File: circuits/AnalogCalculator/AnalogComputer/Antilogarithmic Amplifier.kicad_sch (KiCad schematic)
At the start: 9 parts, among them U4 LM324

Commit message: update circuits
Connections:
- net +12V renamed VCC
- net -12V renamed VSS
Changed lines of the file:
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@@
-    )
-  )
-  (symbol (lib_id "power:+12V") (at 200.66 64.77 0) (unit 1)
-    (in_bom yes) (on_board yes) (dnp no) (fields_autoplaced)
-    (property "Reference" "#PWR04" (at 200.66 68.58 0)
-      (effects (font (size 1.27 1.27)) hide)
-    )
-    (property "Value" "+12V" (at 200.66 61.1942 0)
-      (effects (font (size 1.27 1.27)))
-    )
-    (property "Footprint" "" (at 200.66 64.77 0)
-      (effects (font (size 1.27 1.27)) hide)
-    )
-    (property "Datasheet" "" (at 200.66 64.77 0)
-      (effects (font (size 1.27 1.27)) hide)
-    )
-    (pin "1")
-    (instances
-      (project "AnalogComputer"
-        (path "/923be781-3164-4152-815e-8f20a1ba1c2e/bf1d90c3-cd96-4c8a-a7fb-5bc8190138ca"
-          (reference "#PWR04") (unit 1)
-        )
-        (path "/923be781-3164-4152-815e-8f20a1ba1c2e/3352ab9f-8e2e-464b-bae3-d09535b5c95b"
-          (reference "#PWR013") (unit 1)
-        )
-        (path "/923be781-3164-4152-815e-8f20a1ba1c2e/ca3b0da7-cf56-4357-ae82-a0a8c945f5f8"
-          (reference "#PWR016") (unit 1)
-        )
-      )
     )
   )
@@
     )
   )
+  (symbol (lib_id "power:VSS") (at 215.9 64.77 0) (unit 1)
+    (in_bom yes) (on_board yes) (dnp no) (fields_autoplaced)
+    (property "Reference" "#PWR014" (at 215.9 68.58 0)
+      (effects (font (size 1.27 1.27)) hide)
+    )
+    (property "Value" "VSS" (at 215.9 61.2681 0)
+      (effects (font (size 1.27 1.27)))
+    )
+    (property "Footprint" "" (at 215.9 64.77 0)
+      (effects (font (size 1.27 1.27)) hide)
+    )
+    (property "Datasheet" "" (at 215.9 64.77 0)
+      (effects (font (size 1.27 1.27)) hide)
+    )
+    (pin "1")
+    (instances
+      (project "AnalogComputer"
+        (path "/923be781-3164-4152-815e-8f20a1ba1c2e/bf1d90c3-cd96-4c8a-a7fb-5bc8190138ca"
+          (reference "#PWR014") (unit 1)
+        )
+        (path "/923be781-3164-4152-815e-8f20a1ba1c2e/3352ab9f-8e2e-464b-bae3-d09535b5c95b"
+          (reference "#PWR016") (unit 1)
+        )
+        (path "/923be781-3164-4152-815e-8f20a1ba1c2e/ca3b0da7-cf56-4357-ae82-a0a8c945f5f8"
+          (reference "#PWR017") (unit 1)
+        )
+      )
+    )
+  )
+  (symbol (lib_id "power:VCC") (at 200.66 64.77 0) (unit 1)
+    (in_bom yes) (on_board yes) (dnp no) (fields_autoplaced)
+    (property "Reference" "#PWR04" (at 200.66 68.58 0)
+      (effects (font (size 1.27 1.27)) hide)
+    )
+    (property "Value" "VCC" (at 200.66 61.2681 0)
+      (effects (font (size 1.27 1.27)))
+    )
+    (property "Footprint" "" (at 200.66 64.77 0)
+      (effects (font (size 1.27 1.27)) hide)
+    )
+    (property "Datasheet" "" (at 200.66 64.77 0)
+      (effects (font (size 1.27 1.27)) hide)
+    )
+    (pin "1")
+    (instances
+      (project "AnalogComputer"
+        (path "/923be781-3164-4152-815e-8f20a1ba1c2e/bf1d90c3-cd96-4c8a-a7fb-5bc8190138ca"
+          (reference "#PWR04") (unit 1)
+        )
+        (path "/923be781-3164-4152-815e-8f20a1ba1c2e/3352ab9f-8e2e-464b-bae3-d09535b5c95b"
+          (reference "#PWR05") (unit 1)
+        )
+        (path "/923be781-3164-4152-815e-8f20a1ba1c2e/ca3b0da7-cf56-4357-ae82-a0a8c945f5f8"
+          (reference "#PWR013") (unit 1)
+        )
+      )
+    )
+  )
   (symbol (lib_id "Device:R") (at 144.78 96.52 90) (unit 1)
     (in_bom yes) (on_board yes) (dnp no) (fields_autoplaced)
@@
         )
       )
-    )
-  )
-  (symbol (lib_id "power:-12V") (at 215.9 64.77 0) (unit 1)
-    (in_bom yes) (on_board yes) (dnp no) (fields_autoplaced)
-    (property "Reference" "#PWR05" (at 215.9 62.23 0)
-      (effects (font (size 1.27 1.27)) hide)
-    )
-    (property "Value" "-12V" (at 215.9 61.1942 0)
-      (effects (font (size 1.27 1.27)))
-    )
-    (property "Footprint" "" (at 215.9 64.77 0)
-      (effects (font (size 1.27 1.27)) hide)
-    )
-    (property "Datasheet" "" (at 215.9 64.77 0)
-      (effects (font (size 1.27 1.27)) hide)
-    )
-    (pin "1")
-    (instances
-      (project "AnalogComputer"
-        (path "/923be781-3164-4152-815e-8f20a1ba1c2e/bf1d90c3-cd96-4c8a-a7fb-5bc8190138ca"
-          (reference "#PWR05") (unit 1)
-        )
-        (path "/923be781-3164-4152-815e-8f20a1ba1c2e/3352ab9f-8e2e-464b-bae3-d09535b5c95b"
-          (reference "#PWR014") (unit 1)
-        )
-        (path "/923be781-3164-4152-815e-8f20a1ba1c2e/ca3b0da7-cf56-4357-ae82-a0a8c945f5f8"
-          (reference "#PWR017") (unit 1)
-        )
-      )

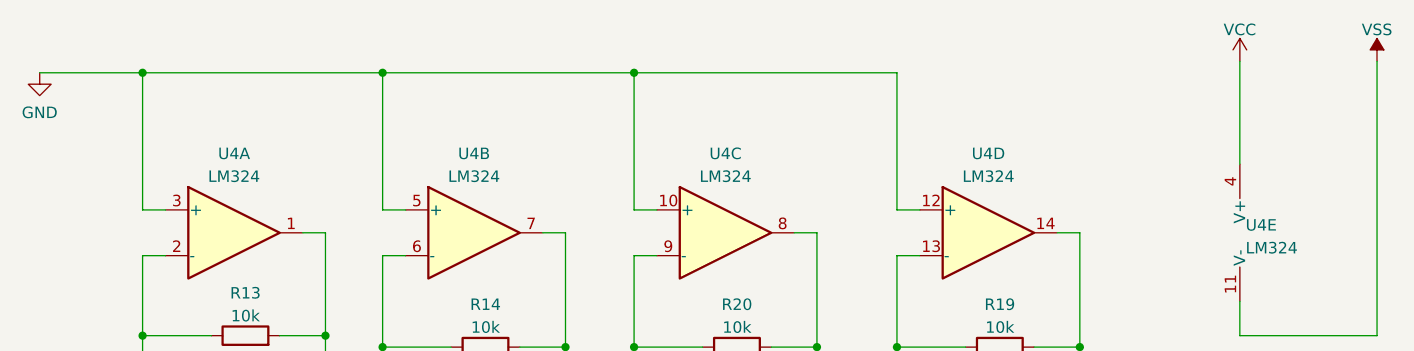
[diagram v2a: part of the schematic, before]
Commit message: update analog computer layout
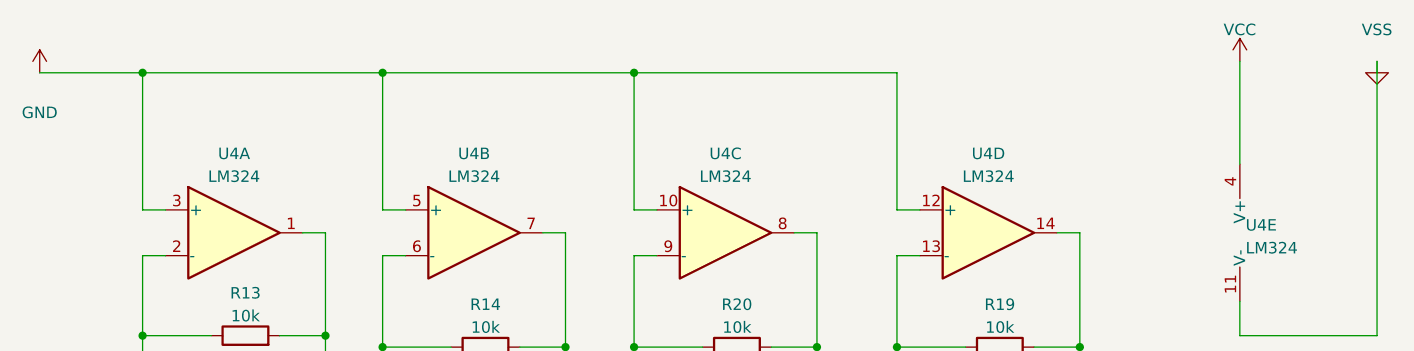
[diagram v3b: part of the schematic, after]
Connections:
- net VSS is gone; now on net GND: U4.11 (V-)
- net GND: no longer U4.10 (+), U4.12 (+), U4.3 (+), U4.5 (+)
- new net VDD: U4.10 (+), U4.12 (+), U4.3 (+), U4.5 (+)
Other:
- company: (none) -> Out-of-band Development, LLC
- title: (none) -> Analog Computer
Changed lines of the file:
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@@
 (kicad_sch (version 20230121) (generator eeschema)
   (paper "A4")
+  (title_block
+    (title "Analog Computer")
+    (date "2023-03-08")
+    (rev "v1")
+    (company "Out-of-band Development, LLC")
+    (comment 1 "Matthew Whited")
+    (comment 2 "Antilogarithmic Amplifer")
+  )
   (junction (at 162.56 96.52) (diameter 0) (color 0 0 0 0)
   )
@@
     )
   )
-  (symbol (lib_id "power:VSS") (at 215.9 64.77 0) (unit 1)
+  (symbol (lib_id "power:GND") (at 215.9 64.77 0) (unit 1)
     (in_bom yes) (on_board yes) (dnp no) (fields_autoplaced)
     (property "Reference" "#PWR014" (at 215.9 68.58 0)
@@
     )
   )
-  (symbol (lib_id "power:GND") (at 67.31 66.04 0) (unit 1)
+  (symbol (lib_id "power:VDD") (at 67.31 66.04 0) (unit 1)
     (in_bom yes) (on_board yes) (dnp no) (fields_autoplaced)
     (property "Reference" "#PWR06" (at 67.31 72.39 0)
